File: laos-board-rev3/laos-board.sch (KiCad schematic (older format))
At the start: 99 parts, among them IC1 KB847, IC2 KB847, J1 USB-A, J10 I2C, J11 MBED NXP, J12 JP, J13 ZEXT, J14 ANALOG, J15 JP, J16 JP_3, J17 POLOLU1201, J18 YAXIS, J19 JP, J2 CAN, J20 YEXT, J21 JP, J22 JP_3, J23 POLOLU1201, J24 XAXIS, J25 JP, J26 XEXT, J27 OUTPUT, J28 VSENSOR, J29 INPUT12, J3 USBPWR, J30 JP, J31 JP_3, J32 POLOLU1201, J33 EAXIS, J34 INPUT34, J35 JP, J36 EEXT, J37 OUTPUT12, J38 VCPU, J39 OUTPUT34, J4 MAGJACK, J40 JP, J41 O1_SRC, J42 O2_SRC, J43 CONN_4, J5 CONN_3, J6 JP, J7 JP_3, J8 POLOLU1201, J9 ZAXIS, P1 FLATCONN, Q1 TIP115, Q2 TIP115, U1 65HVD251, U2 SDCARD, U3 7805

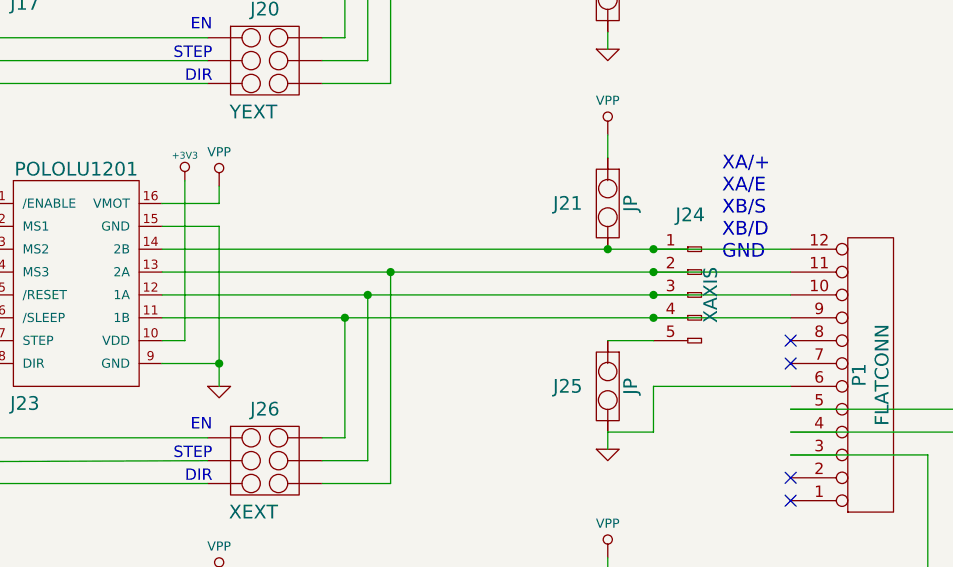
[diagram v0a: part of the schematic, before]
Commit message: version with swapped usb/network
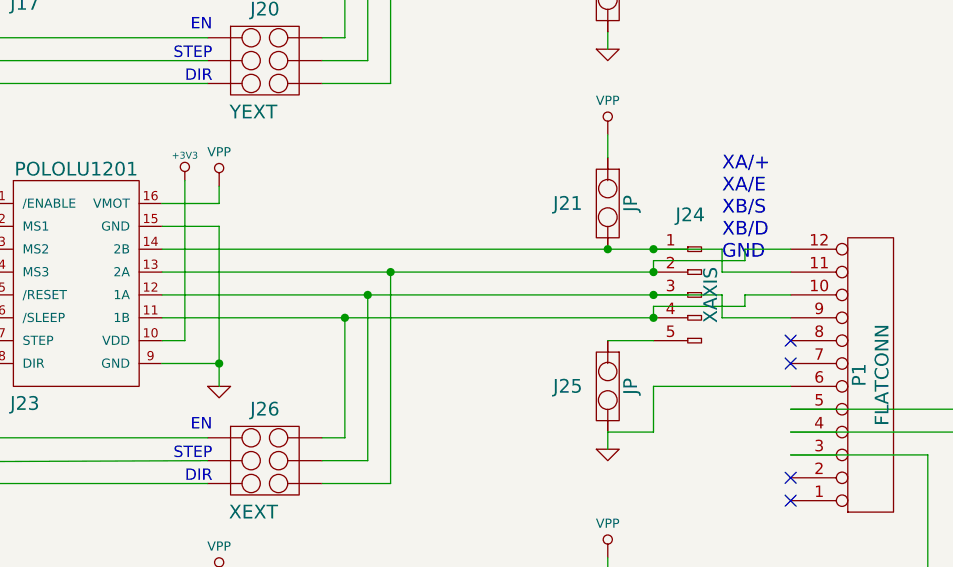
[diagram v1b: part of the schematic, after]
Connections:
- net at J21.2, J23.14 (2B), J24.1 (P1): now also P1.11 (P11); no longer P1.12 (P12)
- net at J23.11 (1B), J24.4 (P4), J26.2 (P6): now also P1.10 (P10); no longer P1.9 (P9)
- net at J23.12 (1A), J24.3 (P3), J26.4 (P5): now also P1.9 (P9); no longer P1.10 (P10)
- net at J23.13 (2A), J24.2 (P2), J26.6 (P4): now also P1.12 (P12); no longer P1.11 (P11)
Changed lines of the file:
@@
-EESchema Schematic File Version 2  date Sat 02 Jun 2012 05:12:06 PM CEST
+EESchema Schematic File Version 2  date Sat 02 Jun 2012 06:00:04 PM CEST
 LIBS:laos_kicad_lib
 LIBS:power
@@
 $EndDescr
 Wire Wire Line
+	10050 6700 12200 6700
+Wire Wire Line
+	10050 6600 12500 6600
+Wire Wire Line
+	10050 6500 12200 6500
+Wire Wire Line
+	10050 6400 12500 6400
+Wire Wire Line
+	12200 6700 12200 6650
+Wire Wire Line
+	12200 6650 12600 6650
+Wire Wire Line
+	12600 6650 12600 6600
+Wire Wire Line
+	12600 6600 12800 6600
+Wire Wire Line
+	12200 6500 12200 6450
+Wire Wire Line
+	12200 6450 12600 6450
+Wire Wire Line
+	12600 6450 12600 6400
+Wire Wire Line
+	12600 6400 12800 6400
+Wire Wire Line
 	12200 4750 10050 4750
 Wire Wire Line
@@
 	12200 7000 12800 7000
 Connection ~ 12200 6700
-Wire Wire Line
-	12800 6700 10050 6700
 Connection ~ 12200 6500
-Wire Wire Line
-	12800 6500 10050 6500
 Connection ~ 1600 8700
 Wire Wire Line
@@
 	-400 8800 1800 8800
 Connection ~ 1600 8800
-Wire Wire Line
-	12800 6400 10050 6400
 Connection ~ 12200 6400
-Wire Wire Line
-	12800 6600 10050 6600
 Connection ~ 12200 6600
 Wire Wire Line
@@
 Wire Wire Line
 	13700 7200 12800 7200
+Wire Wire Line
+	12800 6500 12500 6500
+Wire Wire Line
+	12500 6500 12500 6400
+Wire Wire Line
+	12500 6600 12500 6700
+Wire Wire Line
+	12500 6700 12800 6700
 NoConn ~ 12800 7500
 NoConn ~ 12800 7400
